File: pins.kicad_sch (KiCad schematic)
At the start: 4 parts, among them J3 Conn_01x09, J5 AXK640347YG, J6 Conn_01x40_Pin

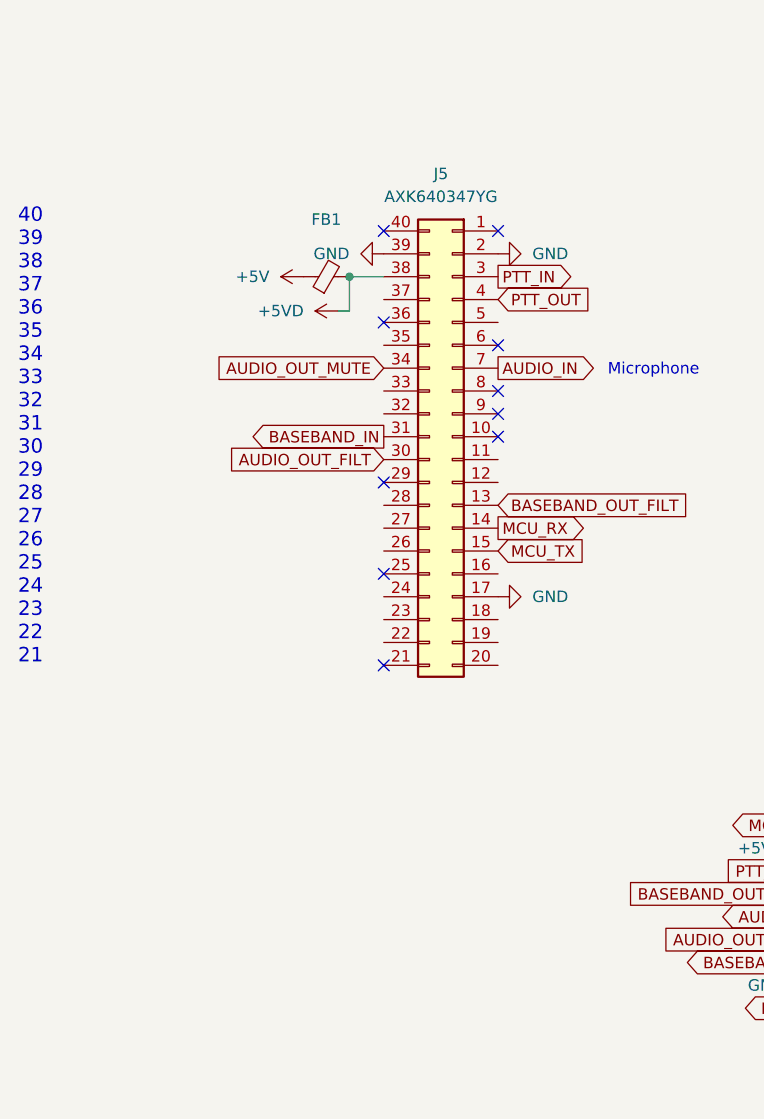
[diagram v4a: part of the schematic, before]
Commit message: J2 Corrected, More TP added.
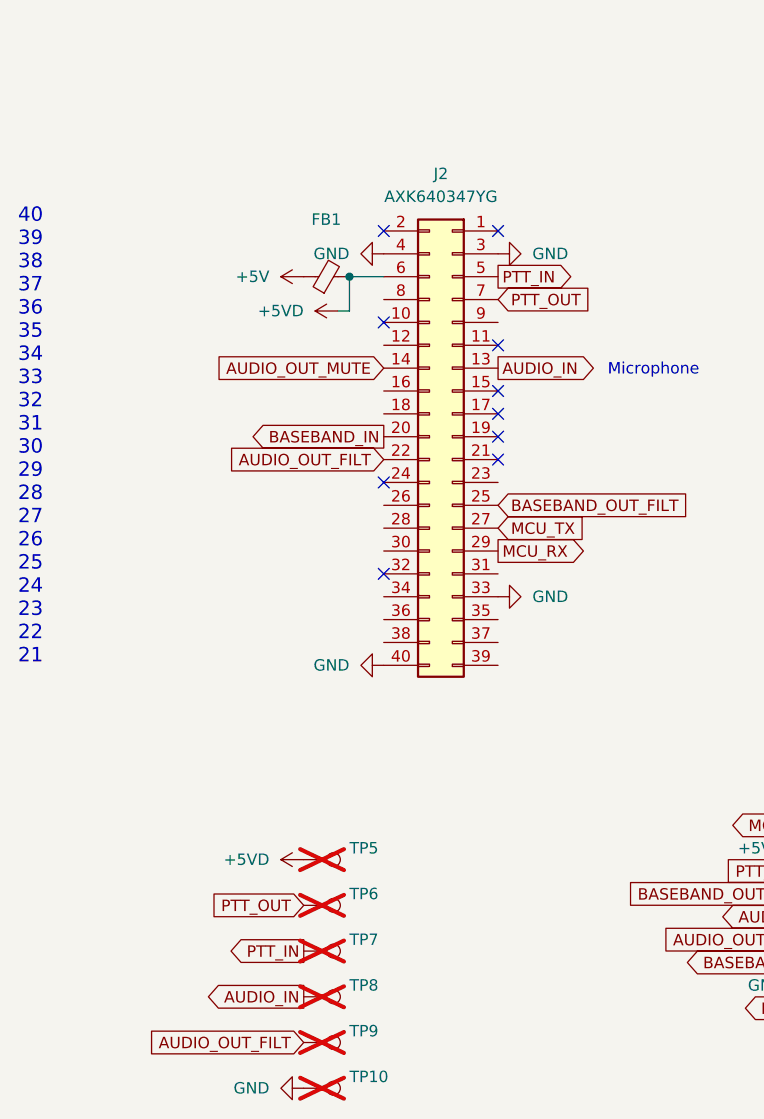
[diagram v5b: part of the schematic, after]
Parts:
- removed J5: AXK640347YG, Micro17-ICOM_Board:AXK640347YG, symbol Connector_Generic:Conn_02x20_Counter_Clockwise
- added J2: AXK640347YG, micro17:AXK640347YG, symbol Connector_Generic:Conn_02x20_Odd_Even
- added TP10, TP5, TP6, TP7, TP8, TP9: GP, TestPoint:TestPoint_Pad_D1.0mm, symbol Connector:TestPoint
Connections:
- net +5VD: now also J2.6 (Pin_6), TP5.1
- net AUDIO_IN: now also J2.13 (Pin_13), TP8.1
- net AUDIO_OUT_FILT: now also J2.22 (Pin_22), TP9.1
- net AUDIO_OUT_MUTE: now also J2.14 (Pin_14)
- net BASEBAND_IN: now also J2.20 (Pin_20)
- net BASEBAND_OUT_FILT: now also J2.25 (Pin_25)
- net GND: now also J2.3 (Pin_3), J2.33 (Pin_33), J2.4 (Pin_4), J2.40 (Pin_40), TP10.1
- net MCU_RX: now also J2.29 (Pin_29)
- net MCU_TX: now also J2.27 (Pin_27)
- net PTT_IN: now also J2.5 (Pin_5), TP7.1
- net PTT_OUT: now also J2.7 (Pin_7), TP6.1

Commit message: PA2 Bias add, USB conn add.
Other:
- title: Micro17 - OpenRTX on a Module -> Micro17 - OpenRTX on a Module for Icom Radios
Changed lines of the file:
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@@
 	(paper "A4")
 	(title_block
-		(title "Micro17 - OpenRTX on a Module")
-		(date "05.12.2023")
+		(title "Micro17 - OpenRTX on a Module for Icom Radios")
+		(date "04.03.2024")
 		(rev "A")
 		(company "Wojciech Kaczmarski SP5WWP et al.")
 		(comment 1 "M17 Project, OpenRTX")
+		(comment 2 "Mano ON6RF")
+		(comment 3 "Mutlu TA1MD")
 	)
 	(junction

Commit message: Changed PA2 bias circuit
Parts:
- FB1: footprint Capacitor_SMD:C_0603_1608Metric -> Inductor_SMD:L_0603_1608Metric_Pad1.05x0.95mm_HandSolder
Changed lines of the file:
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@@
 			)
 		)
-		(property "Footprint" "Capacitor_SMD:C_0603_1608Metric"
+		(property "Footprint" "Inductor_SMD:L_0603_1608Metric_Pad1.05x0.95mm_HandSolder"
 			(at 76.2 58.928 90)
 			(effects

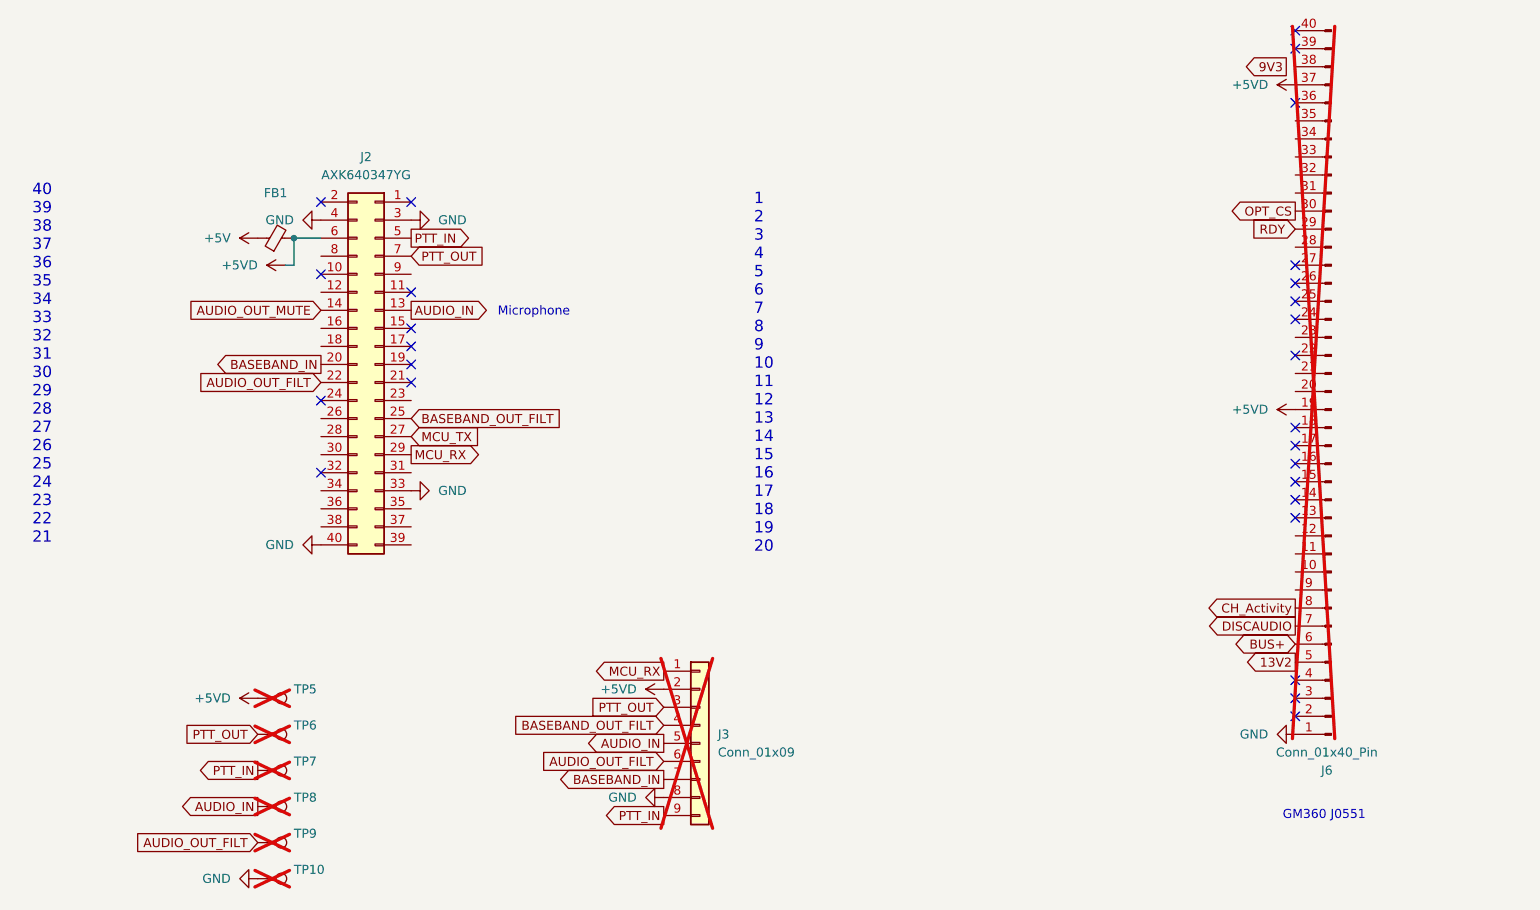
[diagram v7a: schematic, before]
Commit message: cosmetic changes to the schematic layout
- R25 - DNP
- PDF render update
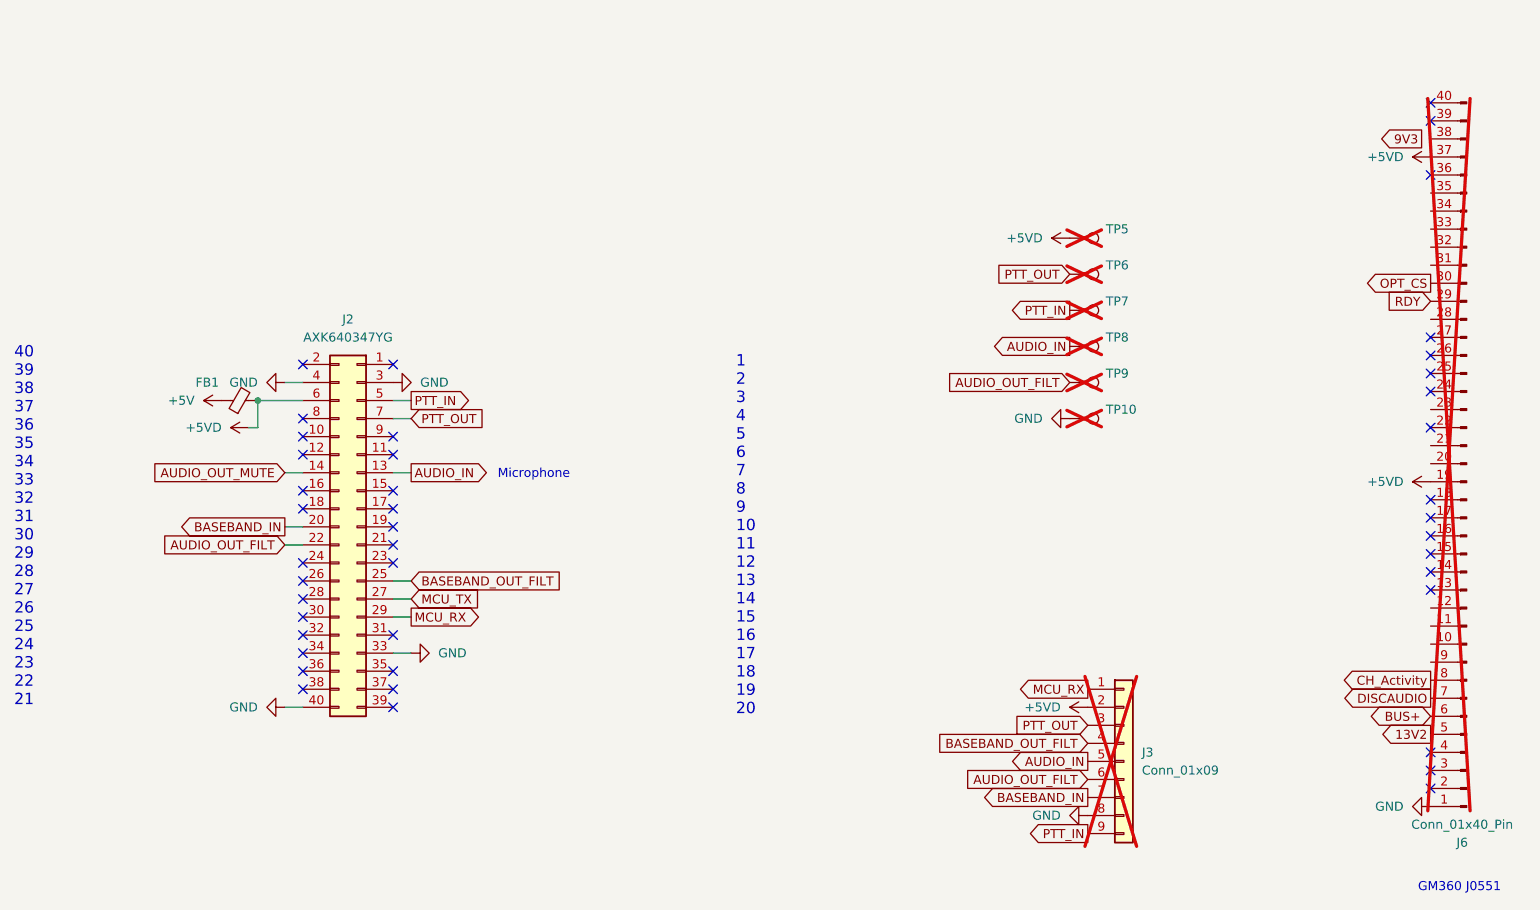
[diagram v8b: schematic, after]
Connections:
- no-connect marks 27 -> 43
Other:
- company: Wojciech Kaczmarski SP5WWP et al. -> Wojciech SP5WWP, Mano ON6RF, Mutlu TA1MD et al.
- title: Micro17 - OpenRTX on a Module for Icom Radios -> Micro17 - OpenRTX on a Module for ICOM radios
- moved on the sheet: FB1, J2, J3, J6, TP10, TP5, TP6, TP7, TP8, TP9
